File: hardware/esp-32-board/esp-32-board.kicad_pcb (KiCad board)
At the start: 2 copper layers, 53.8 x 69.1 mm, 35 parts, among them J1 Conn_Arduino_UNO_R3, J2 Conn_02x03_Odd_Even, J3 ESP-PROG-Program, J4 ESP-PROG-Debug, J5 USB_B_Micro, J6 Barrel_Jack_MountingPin, Q1 BCR129S, SW1 SW_Push, SW2 SW_Push, SW3 SW_DPDT_x2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

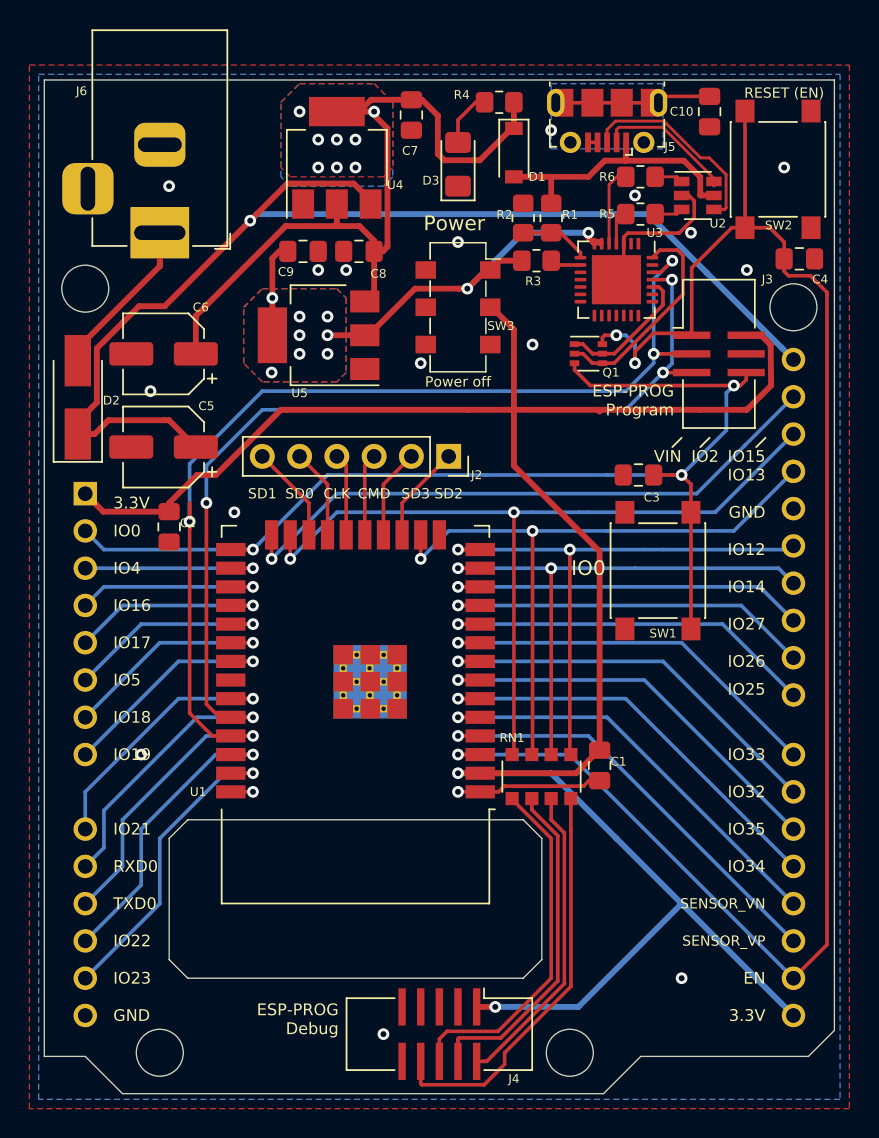
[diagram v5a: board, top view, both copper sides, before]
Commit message: Use FT232RL instead of CP2102N
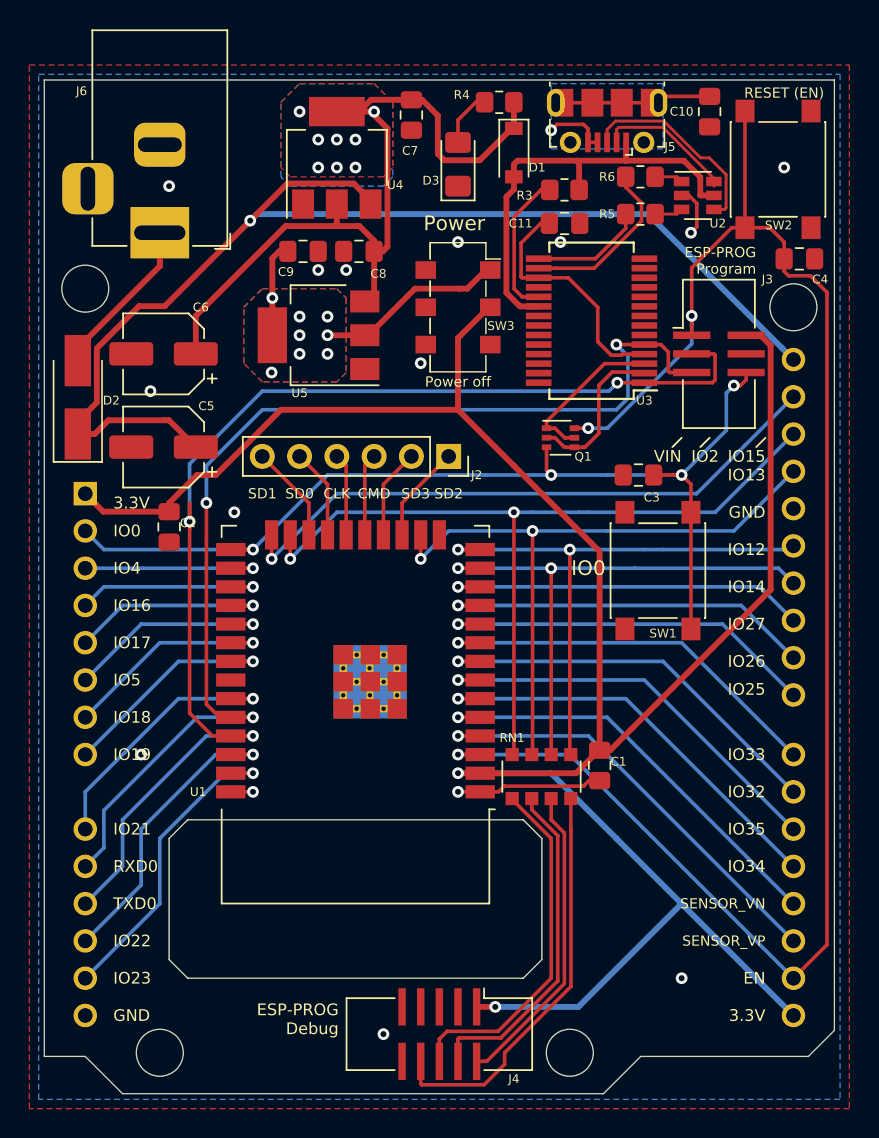
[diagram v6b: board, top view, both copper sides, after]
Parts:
- removed R1: 22k Ohm, Resistor_SMD:R_0805_2012Metric_Pad1.20x1.40mm_HandSolder
- removed R2: 47k Ohm, Resistor_SMD:R_0805_2012Metric_Pad1.20x1.40mm_HandSolder
- added C11: 100nF, Capacitor_SMD:C_0805_2012Metric_Pad1.18x1.45mm_HandSolder, F.Cu at (164.7, 31.1)
- U3: value CP2102N-A01-GQFN28 -> FT232RL; footprint Package_DFN_QFN:QFN-28-1EP_5x5mm_P0.5mm_EP3.35x3.35mm -> Package_SO:SSOP-28_5.3x10.2mm_P0.65mm
- moved Q1 6.04 mm to (164.5, 45.7)
- moved R3 5.19 mm to (164.7, 28.8), turned to 0 degrees
- moved U3 3.27 mm to (166.6, 37.7), turned to 180 degrees
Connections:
- R3 pad 2: /Power/Internal_3V3 -> /USB/VBUS
- U3 pad 1: (no net) -> /TXD0
- U3 pad 15: (no net) -> /USB/USB_DP
- U3 pad 16: (no net) -> /USB/USB_DN
- U3 pad 17: (no net) -> Net-(C11-Pad1)
- U3 pad 18: (no net) -> GND
- U3 pad 19: (no net) -> Net-(R3-Pad1)
- U3 pad 2: (no net) -> /USB/DTR
- U3 pad 20: (no net) -> /USB/VBUS
- U3 pad 21: (no net) -> GND
- U3 pad 24: /USB/RTS -> (no net)
- U3 pad 25: /RXD0 -> GND
- U3 pad 26: /TXD0 -> GND
- U3 pad 28: /USB/DTR -> (no net)
- U3 pad 3: GND -> /USB/RTS
- U3 pad 4: /USB/USB_DP -> Net-(C11-Pad1)
- U3 pad 5: /USB/USB_DN -> /RXD0
- U3 pad 6: /Power/Internal_3V3 -> (no net)
- U3 pad 7: /Power/Internal_3V3 -> GND
- U3 pad 8: Net-(R1-Pad1) -> (no net)
- U3 pad 9: Net-(R3-Pad1) -> (no net)
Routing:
- net Net-(C11-Pad1): track 0.00 -> 16.8 mm
- net /Power/Internal_3V3: track 33.2 -> 19.4 mm, vias 10 -> 8
- net /USB/VBUS: track 18.9 -> 30.3 mm
- net /IO0: track 78.3 -> 68.5 mm, vias 3 -> 4
- net +3V3: track 146.5 -> 156.2 mm
- net Net-(R3-Pad1): track 2.12 -> 10.0 mm
- net /USB/USB_DN: track 5.38 -> 11.8 mm
- net /USB/USB_DP: track 2.63 -> 7.76 mm
- net Net-(R1-Pad1): track 4.80 -> 0.00 mm
- net /TXD0: track 87.5 -> 82.8 mm, vias 4 -> 3
- net /USB/DTR: track 14.7 -> 11.0 mm
- net GND: track 22.9 -> 19.5 mm, vias 18 -> 16
- net /EN: track 113.8 -> 116.5 mm
- net /RXD0: track 80.5 -> 78.2 mm, vias 4 -> 3
- net /USB/RTS: track 9.46 -> 10.9 mm

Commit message: Change connector to simpler (incompatible with Arduino, only similar)
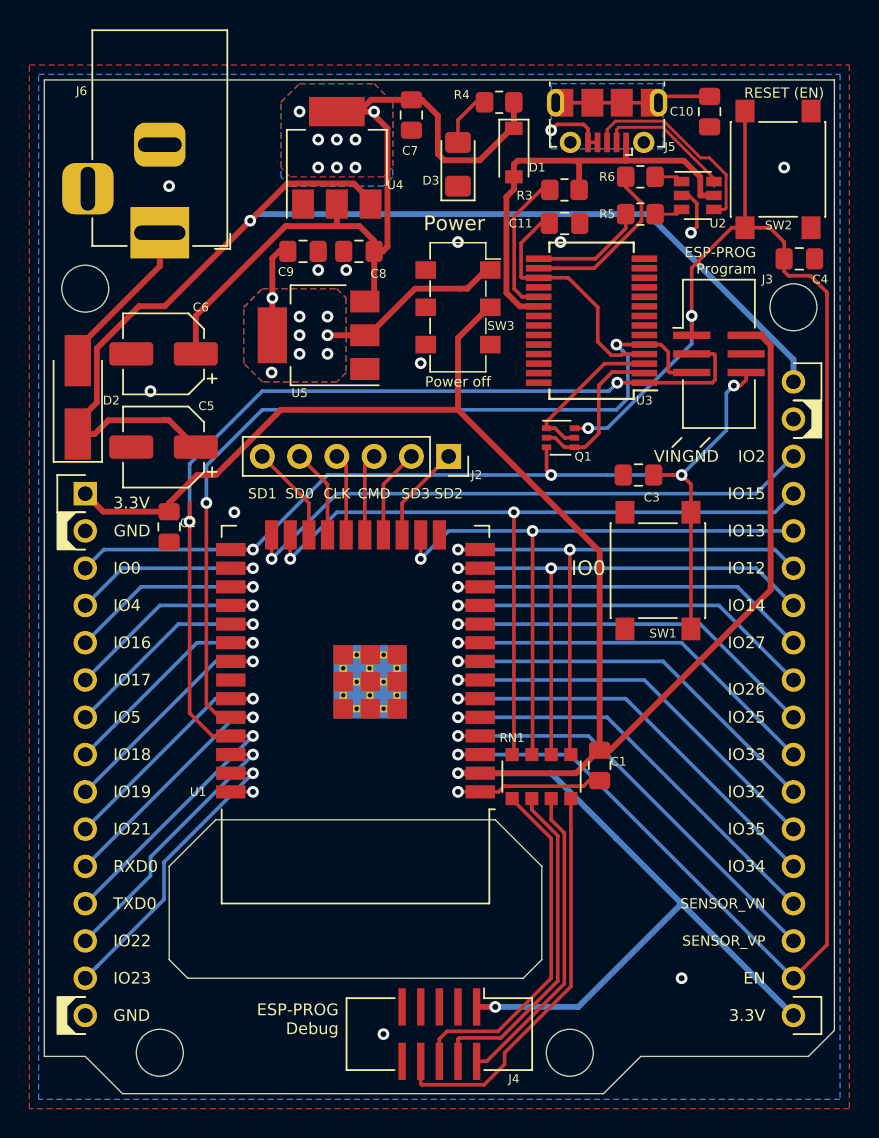
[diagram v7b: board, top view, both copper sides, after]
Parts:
- J1: value Conn_Arduino_UNO_R3 -> MainConnector; footprint Module:Arduino_UNO_R3_WithMountingHoles -> project_components:MainConnector
- J2: value Conn_02x03_Odd_Even -> Conn_01x06
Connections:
- J1 pad 10: /RXD0 -> /IO21
- J1 pad 11: /TXD0 -> /RXD0
- J1 pad 12: /IO22 -> /TXD0
- J1 pad 13: /IO23 -> /IO22
- J1 pad 14: GND -> /IO23
- J1 pad 15: +3V3 -> GND
- J1 pad 16: /EN -> +3V3
- J1 pad 17: /SENSOR_VP -> /EN
- J1 pad 18: /SENSOR_VN -> /SENSOR_VP
- J1 pad 19: /IO34 -> /SENSOR_VN
- J1 pad 2: /IO0 -> GND
- J1 pad 20: /IO35 -> /IO34
- J1 pad 21: /IO32 -> /IO35
- J1 pad 22: /IO33 -> /IO32
- J1 pad 23: /IO25 -> /IO33
- J1 pad 24: /IO26 -> /IO25
- J1 pad 25: /IO27 -> /IO26
- J1 pad 26: /IO14 -> /IO27
- J1 pad 27: /IO12 -> /IO14
- J1 pad 28: GND -> /IO12
- J1 pad 3: /IO4 -> /IO0
- J1 pad 32: VDC -> GND
- J1 pad 4: /IO16 -> /IO4
- J1 pad 5: /IO17 -> /IO16
- J1 pad 6: /IO5 -> /IO17
- J1 pad 7: /IO18 -> /IO5
- J1 pad 8: /IO19 -> /IO18
- J1 pad 9: /IO21 -> /IO19
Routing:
- net /TXD0: track 82.8 -> 80.9 mm
- net /IO2: track 41.8 -> 40.1 mm
- net /IO15: track 56.0 -> 54.3 mm
- net /IO13: track 45.5 -> 43.8 mm
- net VDC: track 80.9 -> 82.4 mm
- net /IO22: track 20.4 -> 18.9 mm
- net /IO21: track 18.1 -> 16.6 mm
- net /RXD0: track 78.2 -> 76.7 mm
- net /IO23: track 21.3 -> 20.2 mm
- net /IO18: track 15.3 -> 16.3 mm
- net /IO4: track 12.9 -> 14.0 mm
- net /IO17: track 14.0 -> 15.0 mm
- net /IO16: track 13.5 -> 14.5 mm
- net /IO19: track 15.6 -> 16.6 mm
- net /IO5: track 14.5 -> 15.6 mm
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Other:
- outline, holes or cut-outs redrawn
